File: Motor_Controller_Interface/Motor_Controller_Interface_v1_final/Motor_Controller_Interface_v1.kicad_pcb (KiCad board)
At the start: 2 copper layers, 67.5 x 45.5 mm, 13 parts, among them J1 NAV_BOARD_INPUT, J2 RMotor, J3 LMotor, J4 5V POWER, Q1 2N3904, Q2 2N3904, U1 74HCT125

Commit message: finalized resistor values, mounting holes added
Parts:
- added REF**: MountingHole_2.7mm_M2.5, MountingHole:MountingHole_2.7mm_M2.5, F.Cu at (188.2, 124.2)
- added REF**: MountingHole_2.7mm_M2.5, MountingHole:MountingHole_2.7mm_M2.5, F.Cu at (144.5, 119.8)
- added REF**: MountingHole_2.7mm_M2.5, MountingHole:MountingHole_2.7mm_M2.5, F.Cu at (189.2, 102.0)
- R2, R4: value rPull -> 1kΩ

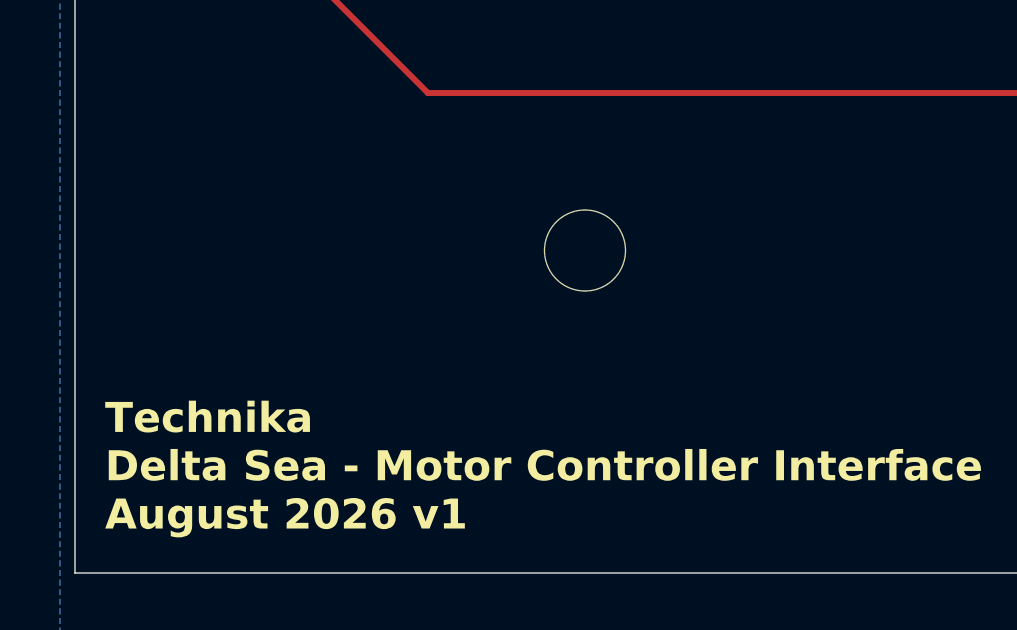
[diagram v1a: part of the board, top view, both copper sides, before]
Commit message: changed naming, adjusted mounting holes
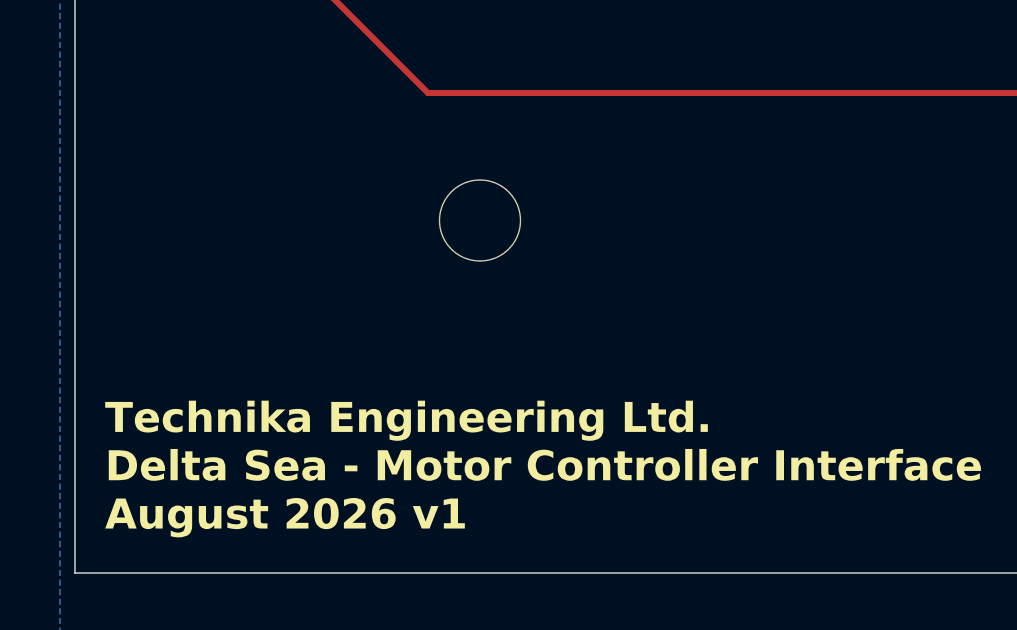
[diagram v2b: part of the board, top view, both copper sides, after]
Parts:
- moved REF** 3.64 mm to (141.0, 118.8)
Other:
- board text added: "Technika Engineering Ltd. Delta Sea - Motor Controller Interface August 2026 v1"
- board text removed: "Technika Delta Sea - Motor Controller Interface August 2026 v1"
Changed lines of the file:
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@@
 			(at 0 3.65 0)
 			(layer "F.Fab")
+			(hide yes)
 			(effects
 				(font
@@
 			(layer "F.CrtYd")
 		)
-		(fp_text user "${REFERENCE}"
-			(at 0 0 0)
-			(layer "F.Fab")
-			(effects
-				(font
-					(size 1 1)
-					(thickness 0.15)
-				)
-			)
-		)
 		(pad "" np_thru_hole circle
 			(at 0 0)
@@
 	(footprint "MountingHole:MountingHole_2.7mm_M2.5"
 		(layer "F.Cu")
-		(at 144.5 119.75)
+		(at 141 118.75)
 		(descr "Mounting Hole 2.7mm, M2.5, no annular, generated by kicad-footprint-generator mountinghole.py")
 		(tags "mountinghole M2.5")
@@
 			(at 0 3.65 0)
 			(layer "F.Fab")
+			(hide yes)
 			(effects
 				(font
@@
 			(layer "F.CrtYd")
 		)
-		(fp_text user "${REFERENCE}"
-			(at 0 0 0)
-			(layer "F.Fab")
-			(effects
-				(font
-					(size 1 1)
-					(thickness 0.15)
-				)
-			)
-		)
 		(pad "" np_thru_hole circle
 			(at 0 0)
@@
 			(at 0 3.65 0)
 			(layer "F.Fab")
+			(hide yes)
 			(effects
 				(font
@@
 			(layer "F.CrtYd")
 		)
-		(fp_text user "${REFERENCE}"
-			(at 0 0 0)
-			(layer "F.Fab")
-			(effects
-				(font
-					(size 1 1)
-					(thickness 0.15)
-				)
-			)
-		)
 		(pad "" np_thru_hole circle
 			(at 0 0)
@@
 		)
 	)
-	(gr_text "Technika\nDelta Sea - Motor Controller Interface\nAugust 2026 v1\n\n"
+	(gr_text "Technika Engineering Ltd.\nDelta Sea - Motor Controller Interface\nAugust 2026 v1\n\n"
 		(at 128.5 130.75 0)
 		(layer "F.SilkS")
